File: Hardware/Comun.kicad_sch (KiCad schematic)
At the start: 7 parts, among them J8 BLUETOOTH, U3 74LVC1G14, U4 SN74LV244A

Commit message: Cambio todos los conectores a SMD
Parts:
- J8: footprint Connector_PinHeader_2.54mm:PinHeader_1x06_P2.54mm_Vertical -> footprints:AMPHENOL_91601-306ALF; PartNumber (none) -> 91601-306ALF; PurchaseLink (none) -> https://www.digikey.com/en/products/detail/amphenol-cs-fci/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
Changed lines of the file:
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@@
 			)
 		)
-		(property "Footprint" "Connector_PinHeader_2.54mm:PinHeader_1x06_P2.54mm_Vertical"
+		(property "Footprint" "footprints:AMPHENOL_91601-306ALF"
 			(at 233.68 46.99 0)
 			(effects
@@
 			)
 		)
-		(property "Datasheet" "~"
+		(property "Datasheet" "https://cdn.amphenol-cs.com/media/wysiwyg/files/drawing/91601.pdf"
 			(at 233.68 46.99 0)
 			(effects
@@
 			)
 		)
-		(property "PartNumber" ""
+		(property "PartNumber" "91601-306ALF"
 			(at 233.68 46.99 0)
 			(effects
@@
 			)
 		)
-		(property "PurchaseLink" ""
+		(property "PurchaseLink" "https://www.digikey.com/en/products/detail/amphenol-cs-fci/91601-306ALF/1539002"
 			(at 233.68 46.99 0)
 			(effects

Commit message: Modifico error del botón en sch y ruteo pistas de potencia
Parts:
- U3: footprint Package_TO_SOT_SMD:SOT-553 -> Package_TO_SOT_SMD:SOT-353_SC-70-5; PartNumber 74LVC1G14Z-7 -> SN74LVC1G14DCKR; PurchaseLink https://www.digikey.com/short/hzhpb2tz -> https://www.digikey.com/en/products/detail/texas-instrument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
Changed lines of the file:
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@@
 			)
 		)
-		(property "Footprint" "Package_TO_SOT_SMD:SOT-553"
+		(property "Footprint" "Package_TO_SOT_SMD:SOT-353_SC-70-5"
 			(at 134.62 102.87 0)
 			(effects
@@
 			)
 		)
-		(property "Datasheet" "https://www.diodes.com/assets/Datasheets/74LVC1G14.pdf"
+		(property "Datasheet" "https://www.ti.com/lit/ds/symlink/sn74lvc1g14.pdf"
 			(at 134.62 109.22 0)
 			(effects
@@
 			)
 		)
-		(property "PartNumber" "74LVC1G14Z-7"
+		(property "PartNumber" "SN74LVC1G14DCKR"
 			(at 134.62 102.87 0)
 			(effects
@@
 			)
 		)
-		(property "PurchaseLink" "https://www.digikey.com/short/hzhpb2tz"
+		(property "PurchaseLink" "https://www.digikey.com/en/products/detail/texas-instruments/SN74LVC1G14DCKR/385725"
 			(at 134.62 102.87 0)
 			(effects

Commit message: Correcciones en el ruteo, agrego fiduciales, 3D y serigrafía
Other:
- company: (none) -> Newsan
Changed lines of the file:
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@@
 	(title_block
 		(title "Archi Bot")
-		(date "2024-07-18")
-		(rev "1.1")
+		(date "2024-09-27")
+		(rev "1.2")
+		(company "Newsan")
 	)
 	(junction

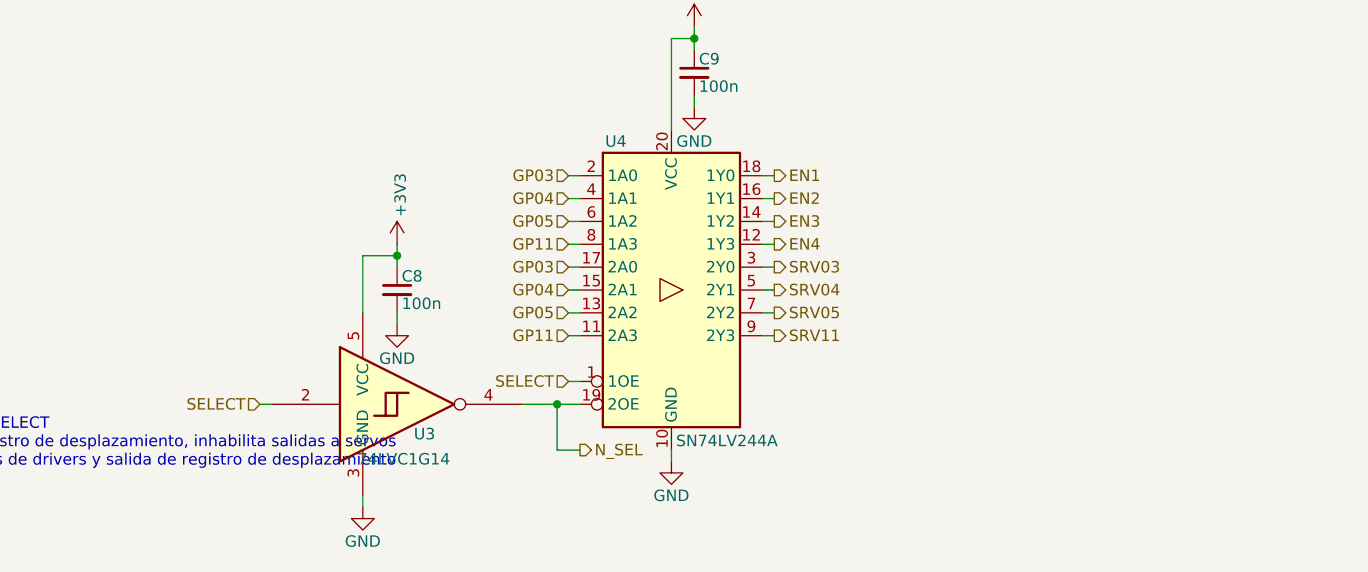
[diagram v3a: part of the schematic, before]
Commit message: Agrego test points, cambio conectores, finalizo v1.2
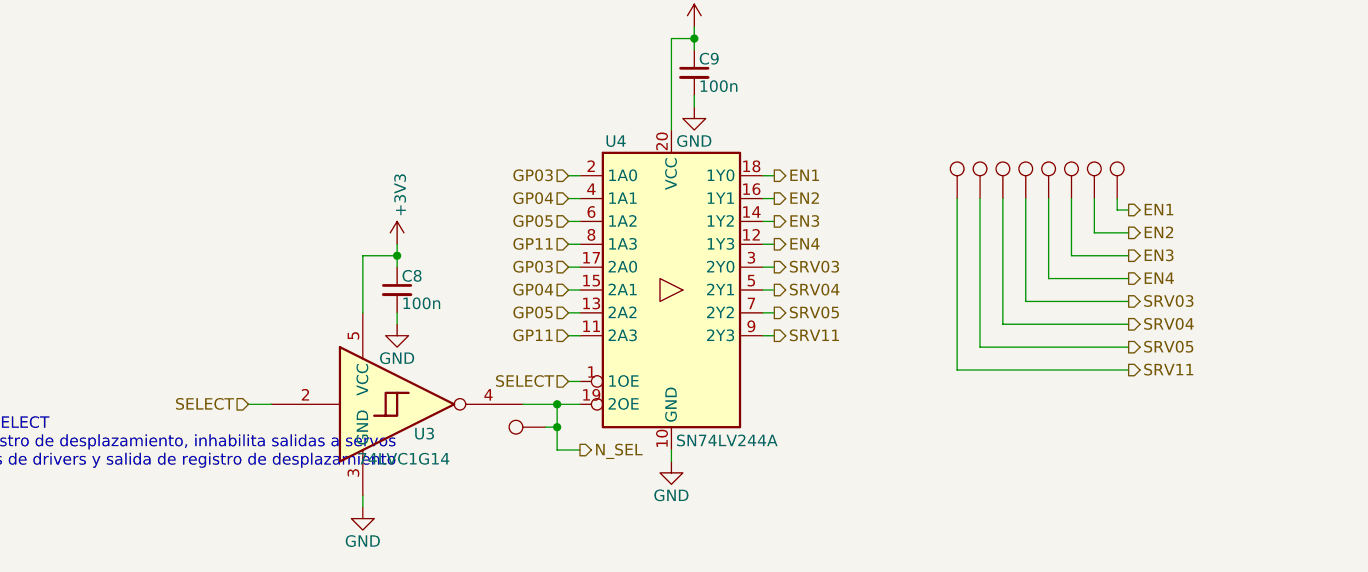
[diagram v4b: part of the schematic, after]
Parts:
- added TP12, TP13, TP14, TP15, TP16, TP17, TP18, TP19, TP7: TestPoint, TestPoint:TestPoint_Pad_D1.0mm, symbol Connector:TestPoint
- J8: footprint footprints:AMPHENOL_91601-306ALF -> footprints:AMPHENOL_91601-306ALF_modif
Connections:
- net EN1: now also TP19.1
- net EN2: now also TP18.1
- net EN3: now also TP17.1
- net EN4: now also TP16.1
- net N_SEL: now also TP7.1
- net SRV03: now also TP15.1
- net SRV04: now also TP14.1
- net SRV05: now also TP13.1
- net SRV11: now also TP12.1

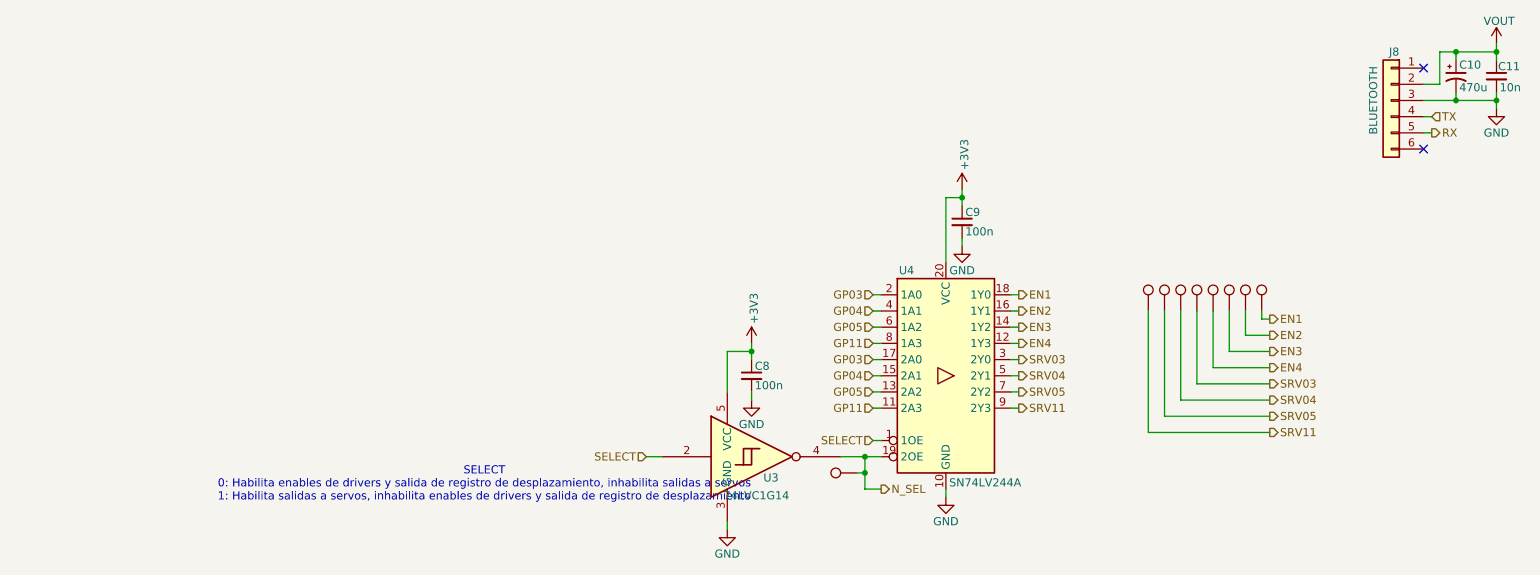
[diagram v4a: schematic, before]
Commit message: Agrego testpoints y modifico footprint de bornera
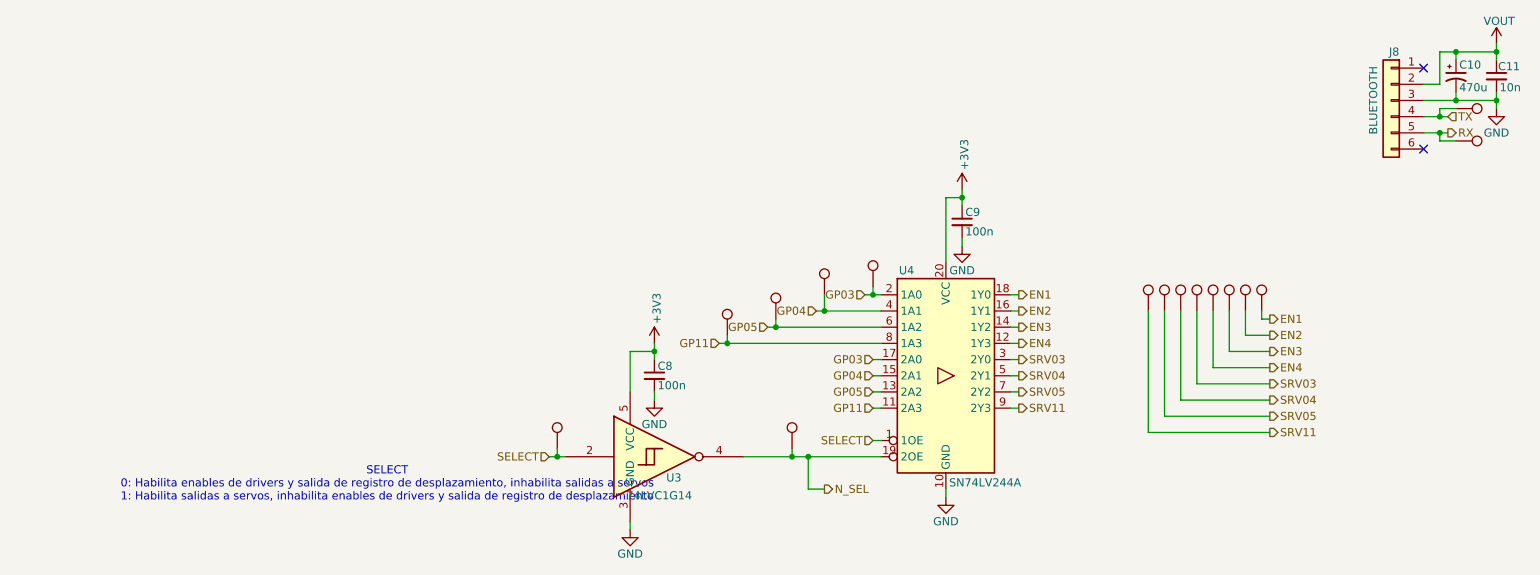
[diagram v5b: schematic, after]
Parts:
- added TP10, TP11, TP30, TP31, TP6, TP8, TP9: TestPoint, TestPoint:TestPoint_Pad_D1.0mm, symbol Connector:TestPoint
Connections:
- net GP03: now also TP10.1
- net GP04: now also TP11.1
- net GP05: now also TP30.1
- net GP11: now also TP31.1
- net RX: now also TP9.1
- net SELECT: now also TP6.1
- net TX: now also TP8.1
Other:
- moved on the sheet: C8, U3

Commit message: Agrego campos manufacturer y package
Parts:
- C10: Manufacturer (none) -> Panasonic Electronic Components; Package (none) -> Radial, Can - SMD (10.30mm x 10.30mm)
- C11: Manufacturer (none) -> Murata Electronics; Package (none) -> 0603 (1608 Metric)
- C8, C9: Manufacturer (none) -> Samsung Electro-Mechanics; Package (none) -> 0603 (1608 Metric)
- J8: Manufacturer (none) -> Amphenol ICC (FCI); Package (none) -> 6POS 0.100" (2.54mm)
- U3: Manufacturer (none) -> Texas Instruments; Package (none) -> 5-TSSOP, SC-70-5, SOT-353
- U4: Manufacturer (none) -> Texas Instruments; Package (none) -> 20-TSSOP (0.173", 4.40mm Width)
